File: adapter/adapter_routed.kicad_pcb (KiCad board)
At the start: 2 copper layers, 31 x 32 mm, 8 parts, among them J1 VP1-055 site, U1 74AHCT245, U2 74AHCT245, U3 74AHCT125

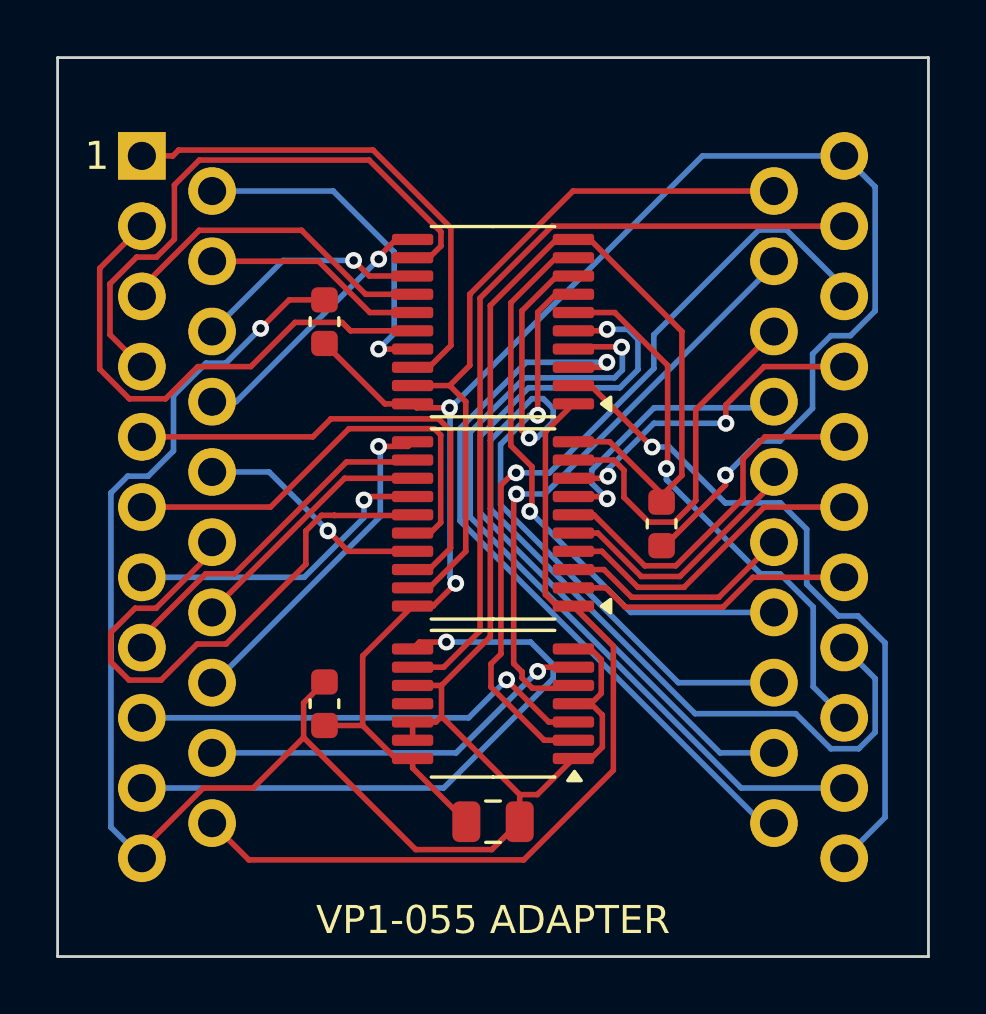
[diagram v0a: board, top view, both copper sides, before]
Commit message: adapter rev B: pin field 11-10-11-10 (sides are translated copies, not mirrored)
Rev A mirrored the right-hand side and did not fit the socketed site.
Re-routed (357 segments, 22 vias, DRC clean), REV B silk mark on both
sides, finish_adapter restores the design rules before DRC, run.sh SVG
export uses the right layer name.

Co-Authored-By: Claude Fable 5.1 <noreply@anthropic.com>
Claude-Session: https://claude.ai/code/session_01Vag23esQ6CiLGDPZcUdJPn
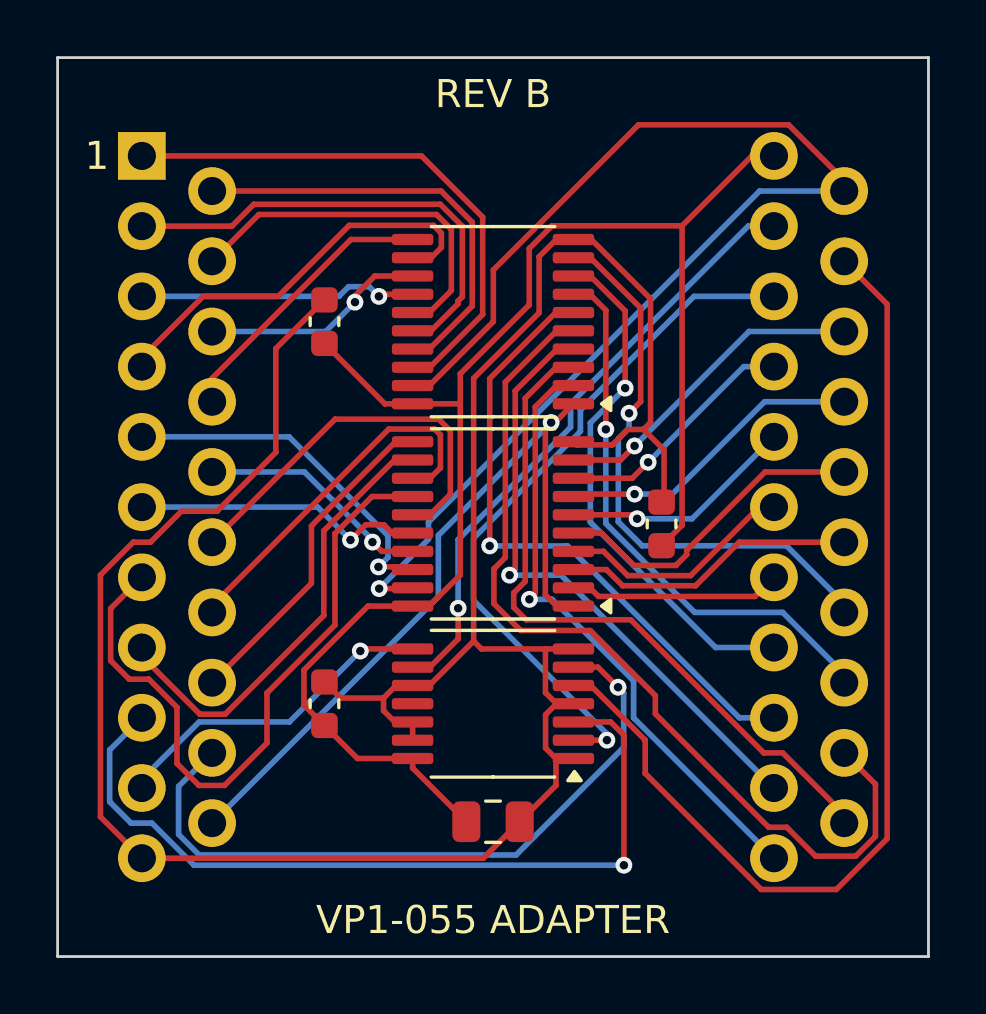
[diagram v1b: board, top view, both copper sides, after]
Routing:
- net nOE: track 25.8 -> 45.5 mm, vias 0 -> 1
- net nA6: track 34.9 -> 18.8 mm
- net C1: track 21.4 -> 36.8 mm, vias 1 -> 0
- net W4: track 11.2 -> 24.4 mm, vias 1 -> 0
- net A0: track 16.5 -> 29.3 mm
- net A1: track 14.1 -> 25.2 mm
- net A2: track 22.2 -> 11.9 mm
- net nA2: track 29.2 -> 21.9 mm
- net C2: track 28.8 -> 21.9 mm, vias 0 -> 1
- net GND: track 96.2 -> 89.8 mm, vias 1 -> 0
- net V6: track 20.9 -> 14.7 mm
- net W3: track 20.3 -> 14.4 mm
- net nA3: track 26.9 -> 32.6 mm, vias 1 -> 0
- net W2: track 16.2 -> 10.5 mm, vias 0 -> 1
- net V3: track 7.89 -> 13.3 mm
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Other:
- board text added: "REV B"

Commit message: adapter rev C: pin field 10-11-10-11, pin 1 in the inner row
Counted on the socketed site with pin 1 top-left: the sides are translated
copies and the 11-pin row is inboard on the pin-1 side. Rev A's right side
already fitted; only the left side's two rows swap. Re-routed (362
segments, 22 vias, DRC clean), REV C silk on both sides, pin-1 marker
directly above the square pad.

Co-Authored-By: Claude Fable 5.1 <noreply@anthropic.com>
Claude-Session: https://claude.ai/code/session_01Vag23esQ6CiLGDPZcUdJPn
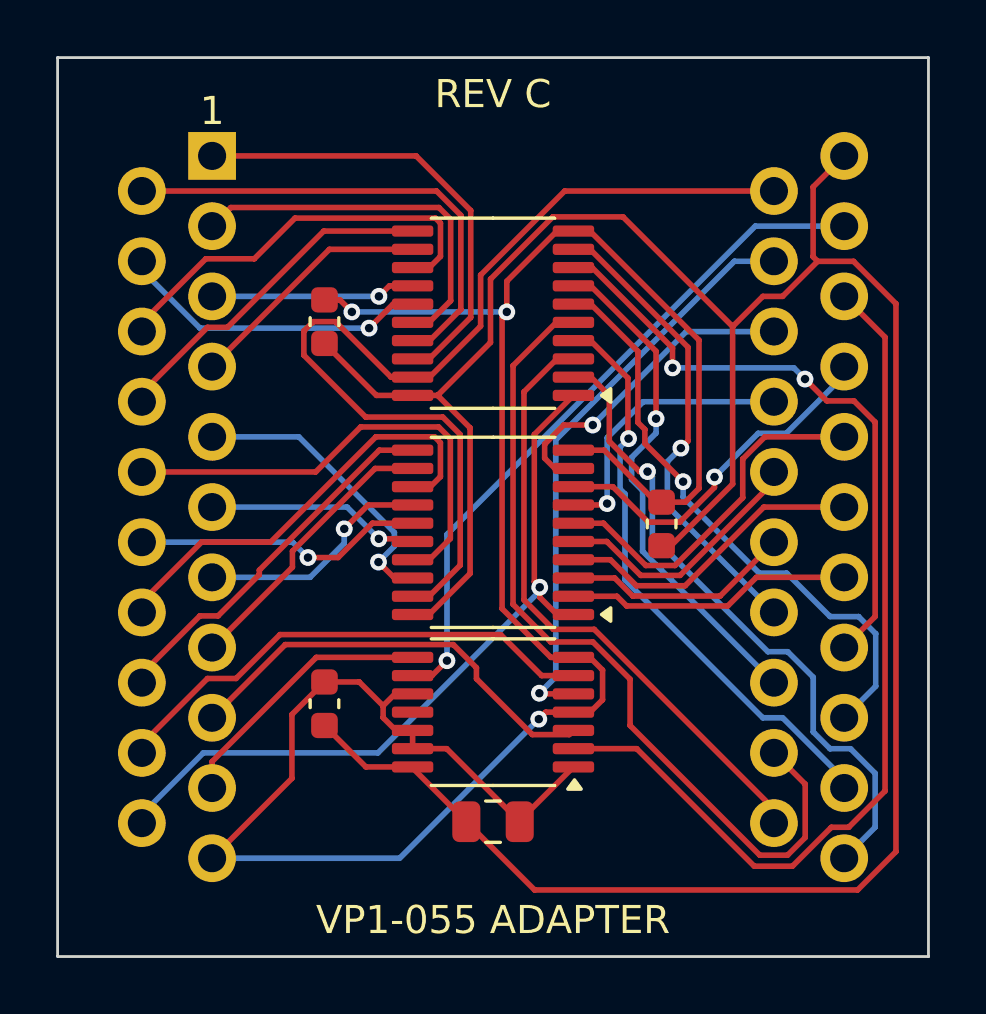
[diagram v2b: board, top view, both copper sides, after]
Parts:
- moved U3 0.30 mm to (0.00, 7.30)
- moved U1 0.30 mm to (0.00, -6.90)
- moved U2 0.30 mm to (0.00, 0.90)
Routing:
- net VCC: track 56.0 -> 93.9 mm
- net C1: track 36.8 -> 20.9 mm, vias 0 -> 1
- net W4: track 24.4 -> 8.50 mm, vias 0 -> 1
- net A0: track 29.3 -> 15.6 mm, vias 1 -> 0
- net nOE: track 45.5 -> 35.9 mm, vias 1 -> 0
- net W1: track 8.35 -> 17.0 mm, vias 1 -> 0
- net GND: track 89.8 -> 81.6 mm, vias 0 -> 3
- net A1: track 25.2 -> 17.9 mm, vias 1 -> 0
- net C0: track 25.1 -> 32.1 mm, vias 1 -> 0
- net V5: track 8.09 -> 14.9 mm, vias 1 -> 0
- net W6: track 16.3 -> 10.1 mm
- net V6: track 14.7 -> 8.87 mm
- net nA12: track 8.40 -> 13.0 mm, vias 1 -> 0
- net nA14: track 8.78 -> 12.9 mm
- net W3: track 14.4 -> 10.4 mm, vias 0 -> 1
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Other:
- board text added: "REV C"
- board text removed: "REV B"

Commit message: adapter rev C: routing polish - 0.7 mm vias, wider power, GND pours, decoupling next to VCC pins
Pin field unchanged (drill file identical to the previous rev C). Rerouted
with 0.2 mm via rings and C2 moved beside U2's VCC pin; polish_adapter.py
widens VCC/GND where clearance allows and adds GND pours on both layers.
README gets a routing-practice checklist against the JLCPCB rules.

Co-Authored-By: Claude Fable 5.1 <noreply@anthropic.com>
Claude-Session: https://claude.ai/code/session_01Vag23esQ6CiLGDPZcUdJPn
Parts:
- moved C2 12.0 mm to (-6.00, 0.60)
- moved U3 0.30 mm to (0.00, 7.00)
- moved U1 0.30 mm to (0.00, -6.60)
- moved U2 0.30 mm to (0.00, 0.60)
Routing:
- net VCC: track 93.9 -> 48.2 mm, vias 0 -> 1
- net nA3: track 30.1 -> 18.3 mm
- net W3: track 10.4 -> 20.7 mm, vias 1 -> 0
- net A0: track 15.6 -> 25.0 mm
- net DIR: track 27.2 -> 36.6 mm, vias 1 -> 0
- net GND: track 81.6 -> 90.5 mm, vias 3 -> 1
- net nA10: track 11.2 -> 19.4 mm, vias 0 -> 1
- net nA14: track 12.9 -> 20.7 mm
- net C0: track 32.1 -> 24.9 mm, vias 0 -> 1
- net V4: track 7.29 -> 14.0 mm, vias 1 -> 0
- net V3: track 11.2 -> 17.5 mm, vias 1 -> 0
- net W1: track 17.0 -> 10.8 mm, vias 0 -> 1
- net W2: track 7.64 -> 13.7 mm, vias 1 -> 0
- net W0: track 10.6 -> 14.8 mm, vias 1 -> 0
- net C2: track 24.6 -> 28.5 mm, vias 1 -> 0
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- added copper zone on B.Cu, net GND
- added copper zone on F.Cu, net GND
